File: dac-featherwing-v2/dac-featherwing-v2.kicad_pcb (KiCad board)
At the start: 2 copper layers, 43.2 x 58.4 mm, 36 parts, among them J1 BOT, J2 TOP, J3 AudioJack4, J4 AudioJack4, U1 WM8731CLSEFL

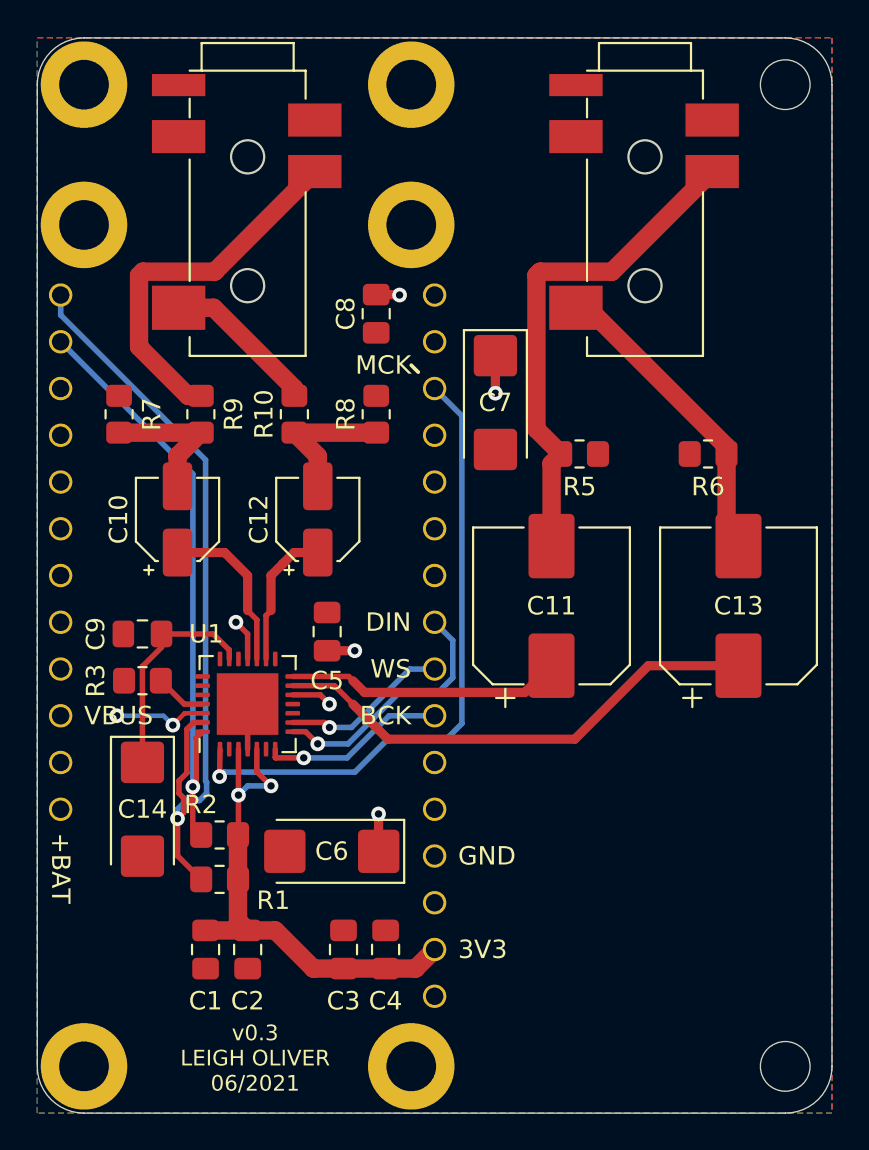
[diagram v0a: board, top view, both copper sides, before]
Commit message: Redid routing to be much better
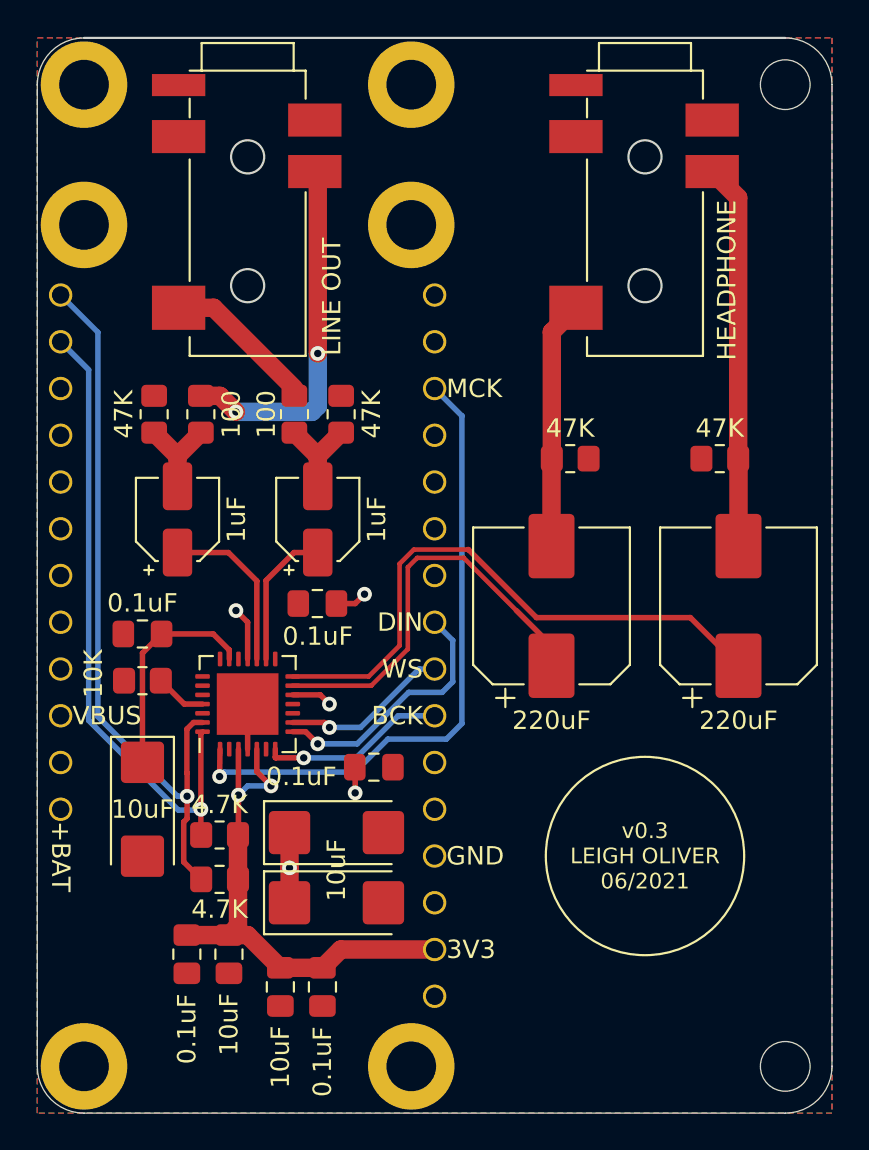
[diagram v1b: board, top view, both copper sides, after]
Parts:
- J3: value AudioJack4 -> HEADPHONE
- J4: value AudioJack4 -> LINE OUT
- moved C7 24.9 mm to (125.2, 98.6), turned to 0 degrees
- moved C8 24.6 mm to (127.3, 95.1), turned to 0 degrees
- moved C3 3.99 mm to (122.2, 107.0), turned to -90 degrees
- moved C4 3.99 mm to (124.5, 107.0), turned to -90 degrees
- moved C6 2.81 mm to (125.2, 102.4), turned to 0 degrees
- moved R7 1.91 mm to (115.3, 75.9)
- moved R8 1.91 mm to (125.5, 75.9)
- moved C5 1.61 mm to (124.2, 86.2), turned to 180 degrees
- moved C1 1.05 mm to (117.1, 105.2)
- moved C2 1.05 mm to (119.4, 105.2)
- moved R6 0.68 mm to (146.1, 78.3)
- moved R5 0.57 mm to (137.9, 78.3)
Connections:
- C11 pad 1: Net-(C11-Pad1) -> Net-(U1-Pad13)
- C11 pad 2: RHPOUT -> LHPOUT
- C13 pad 1: Net-(C13-Pad1) -> Net-(U1-Pad14)
- C13 pad 2: LHPOUT -> RHPOUT
- R5 pad 2: RHPOUT -> LHPOUT
- R6 pad 1: LHPOUT -> RHPOUT
- U1 pad 13: Net-(C13-Pad1) -> Net-(U1-Pad13)
- U1 pad 14: Net-(C11-Pad1) -> Net-(U1-Pad14)
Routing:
- net Net-(U1-Pad14): track 0.00 -> 32.3 mm
- net Net-(C13-Pad1): track 27.1 -> 0.00 mm
- net Net-(U1-Pad13): track 0.00 -> 22.6 mm
- net Net-(C11-Pad1): track 15.0 -> 0.00 mm
- net RHPOUT: track 27.4 -> 21.9 mm
- net GND: track 7.59 -> 2.45 mm, vias 2 -> 0
- net SDA: track 42.9 -> 40.0 mm
- net LHPOUT: track 17.0 -> 14.1 mm
- net Net-(C12-Pad2): track 7.89 -> 5.24 mm
- net Net-(C10-Pad2): track 7.89 -> 5.24 mm
- net SCL: track 33.3 -> 35.0 mm
- net +3V3: track 28.1 -> 29.6 mm
- net +3.3VA: track 11.3 -> 12.0 mm, vias 6 -> 5
- net ROUT: track 20.2 -> 19.6 mm, vias 0 -> 2

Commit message: DACV2 Complete. Ordered. Checked other files.
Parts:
- added 3V3A SRC: 3V3A SRC, Jumper:SolderJumper-3_P2.0mm_Open_TrianglePad1.0x1.5mm_NumberLabels, B.Cu at (134.4, 85.9)
- J3: value HEADPHONE -> SPK
- J4: value LINE OUT -> LINE
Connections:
- J1 pad 1: +3.3VA -> +3.3VDAC
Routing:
- net +3V3: track 29.6 -> 48.2 mm
- net +3.3VDAC: track 0.00 -> 16.1 mm
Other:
- board text added: "3V3A"
- board text added: "I2C DAC FEATHERWING"
- board text added: "SCL"
- board text added: "SDA"
- board text removed: "+BAT"
- board text removed: "VBUS"
